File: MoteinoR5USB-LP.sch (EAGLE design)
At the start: 33 parts, among them CN1 MINIB, IC3 MCP1703CB, U1 FT231XS, U3 SN74LVC1T45, X1 16 MHz

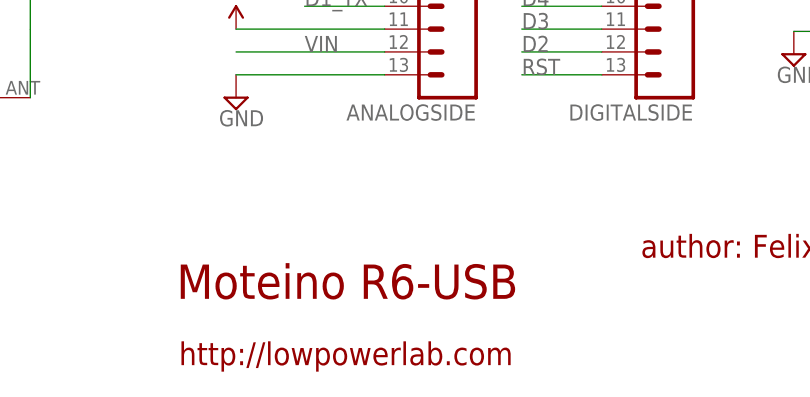
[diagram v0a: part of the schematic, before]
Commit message: Added a MOSFET variant
- replaced voltage shifter with mosfet
- some trace & silkscreen adjustments on both boards
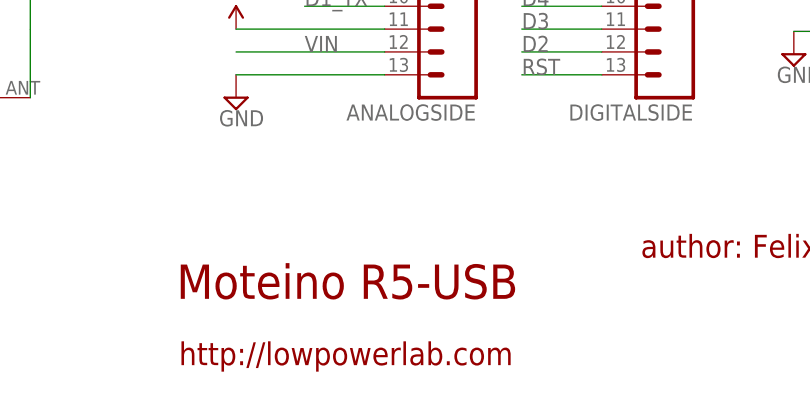
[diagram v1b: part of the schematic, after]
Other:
- note added: "Moteino R5-USB"
- note removed: "Moteino R6-USB"
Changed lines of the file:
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@@
 <?xml version="1.0" encoding="utf-8"?>
 <!DOCTYPE eagle SYSTEM "eagle.dtd">
-<eagle version="8.2.0">
+<eagle version="8.5.1">
 <drawing>
 <settings>
 <setting alwaysvectorfont="no"/>
+<setting keepoldvectorfont="yes"/>
 <setting verticaltext="up"/>
 </settings>
@@
 <sheet>
 <plain>
-<text x="166.116" y="15.748" size="3.81" layer="94" font="vector" ratio="10">Moteino R6-USB</text>
+<text x="166.116" y="15.748" size="3.81" layer="94" font="vector" ratio="10">Moteino R5-USB</text>
 <text x="217.678" y="20.32" size="2.54" layer="94" font="vector">author: Felix Rusu</text>
 <text x="166.37" y="8.382" size="2.54" layer="94" font="vector">http://lowpowerlab.com</text>
@@
 <compatibility>
 <note version="8.2" severity="warning">
-Since Version 8.2, Eagle supports online libraries. The ids
+Since Version 8.2, EAGLE supports online libraries. The ids
 of those online libraries will not be understood (or retained)
 with this version.
